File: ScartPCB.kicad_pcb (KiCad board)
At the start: 4 copper layers, 39.5 x 21 mm, 55 parts, among them J1 Conn_02x10_Odd_Even, Q1 BC847W, Q2 BC857W, U1 TPS61040DBVR

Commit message: Change it to work more like I want it to
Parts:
- removed C1: 4.7uF, Capacitor_SMD:C_0402_1005Metric
- removed C2: 10pF, Capacitor_SMD:C_0402_1005Metric
- removed C3: 1uF, Capacitor_SMD:C_0402_1005Metric
- removed C4: 100nF, Capacitor_SMD:C_0402_1005Metric
- removed CB2, CC2, CG2, CR2: 100uF, Capacitor_SMD:C_1206_3216Metric
- removed CB3, CC3, CG3, CR3: 22uF, Capacitor_SMD:C_0603_1608Metric
- removed D1, D2: D_Schottky, Diode_SMD:D_0402_1005Metric
- removed L1: 10uH, Inductor_SMD:L_0603_1608Metric
- removed Q1: BC847W, Package_TO_SOT_SMD:SOT-323_SC-70
- removed Q2: BC857W, Package_TO_SOT_SMD:SOT-323_SC-70
- removed R1: 1.6M, Resistor_SMD:R_0402_1005Metric
- removed R2: 200K, Resistor_SMD:R_0402_1005Metric
- removed R3: 1K, Resistor_SMD:R_0402_1005Metric
- removed R5, R6: 1M, Resistor_SMD:R_0402_1005Metric
- C0: footprint Capacitor_SMD:C_0402_1005Metric -> Capacitor_SMD:C_0805_2012Metric_Pad1.18x1.45mm_HandSolder
- CB1, CG1, CR1: value 100uF -> C_Polarized; footprint Capacitor_SMD:C_1206_3216Metric -> Capacitor_Tantalum_SMD:CP_EIA-3528-21_Kemet-B_HandSolder
- CC1: value 100uF -> 220uF; footprint Capacitor_SMD:C_1206_3216Metric -> Capacitor_Tantalum_SMD:CP_EIA-3528-21_Kemet-B_HandSolder
- R7, R9, RB1, RB2, RC2, RG1, RG2, RR1, RR2: footprint Resistor_SMD:R_0402_1005Metric -> Resistor_SMD:R_0805_2012Metric_Pad1.20x1.40mm_HandSolder
- R8: footprint Resistor_SMD:R_0402_1005Metric -> Resistor_SMD:R_0805_2012Metric_Pad1.20x1.40mm_HandSolder; moved to F.Cu
- RC1: value 300 -> 470; footprint Resistor_SMD:R_0402_1005Metric -> Resistor_SMD:R_0805_2012Metric_Pad1.20x1.40mm_HandSolder
- U1: value TPS61040DBVR -> 74LVC1G17; footprint Footprints:TPS61040DBVR -> Package_TO_SOT_SMD:SC-74A-5_1.55x2.9mm_P0.95mm
- moved U1 14.7 mm to (140.3, 115.0), turned to 180 degrees
- moved R9 12.1 mm to (148.5, 117.5)
- moved RR1 9.16 mm to (146.5, 114.0), turned to 180 degrees
- moved RG1 6.19 mm to (151.0, 114.0), turned to 180 degrees
- moved RC1 6.01 mm to (132.5, 116.5)
- moved RR2 5.63 mm to (143.5, 113.5), turned to -90 degrees
- moved RB1 5.58 mm to (158.0, 114.0), turned to 180 degrees
- moved CB1 4.36 mm to (158.6, 117.0), turned to 0 degrees
- moved RB2 4.29 mm to (151.5, 109.5)
- moved CR1 3.94 mm to (145.5, 117.0), turned to 0 degrees
- moved RG2 2.97 mm to (147.5, 111.5), turned to 0 degrees
- moved CG1 2.96 mm to (152.0, 117.0), turned to 0 degrees
- moved R7 2.36 mm to (136.0, 115.5)
- moved C0 2.25 mm to (156.5, 111.5), turned to 0 degrees
- moved R8 1.55 mm to (138.5, 116.0)
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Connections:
- J1 pad 13: unconnected-(J1-Pad13) -> GND
- J1 pad 14: unconnected-(J1-Pad14) -> GND
- J1 pad 4: unconnected-(J1-Pad4) -> GND
- J1 pad 5: unconnected-(J1-Pad5) -> GND
- J1 pad 8: SWITCH -> unconnected-(J1-Pin_8-Pad8)
- J1 pad 9: unconnected-(J1-Pad9) -> GND
- R7 pad 1: Net-(CC1-Pad2) -> Net-(CC1-Pad1)
- R8 pad 1: Net-(CC1-Pad2) -> Net-(CC1-Pad1)
- RC1 pad 2: Net-(CC1-Pad1) -> Net-(CC1-Pad2)
- U1 pad 1: Net-(D2-Pad2) -> unconnected-(U1-NC-Pad1)
- U1 pad 2: GND -> C
- U1 pad 3: Net-(C2-Pad2) -> GND
- U1 pad 4: Net-(C1-Pad1) -> C_SYNC
- U1 pad 5: Net-(C1-Pad1) -> +5V
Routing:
- net RGB_BLANKING: track 3.41 -> 14.5 mm
- net Net-(CC1-Pad2): track 13.2 -> 3.41 mm
- net Net-(JP2-B): track 14.3 -> 5.61 mm
- net B: track 8.77 -> 16.8 mm
- net Net-(C4-Pad2): track 7.12 -> 0.00 mm
- net RED: track 6.86 -> 13.9 mm
- net Net-(C1-Pad1): track 6.54 -> 0.00 mm
- net GREEN: track 6.68 -> 12.7 mm
- net Net-(CC1-Pad1): track 12.1 -> 6.52 mm
- net BLUE: track 6.68 -> 11.7 mm
- net Net-(C2-Pad1): track 4.66 -> 0.00 mm
- net Net-(C2-Pad2): track 4.48 -> 0.00 mm
- net Net-(D2-Pad2): track 3.85 -> 0.00 mm
- net SWITCH: track 3.66 -> 0.00 mm
- net Net-(CB1-Pad1): track 5.79 -> 3.00 mm
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- removed copper zone on B.Cu, net +5V
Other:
- board text added: "V1.0"
- board text added: "github/ dottedquad"
- board text removed: "V2.0"
- board text removed: "github/ screwbreaker"

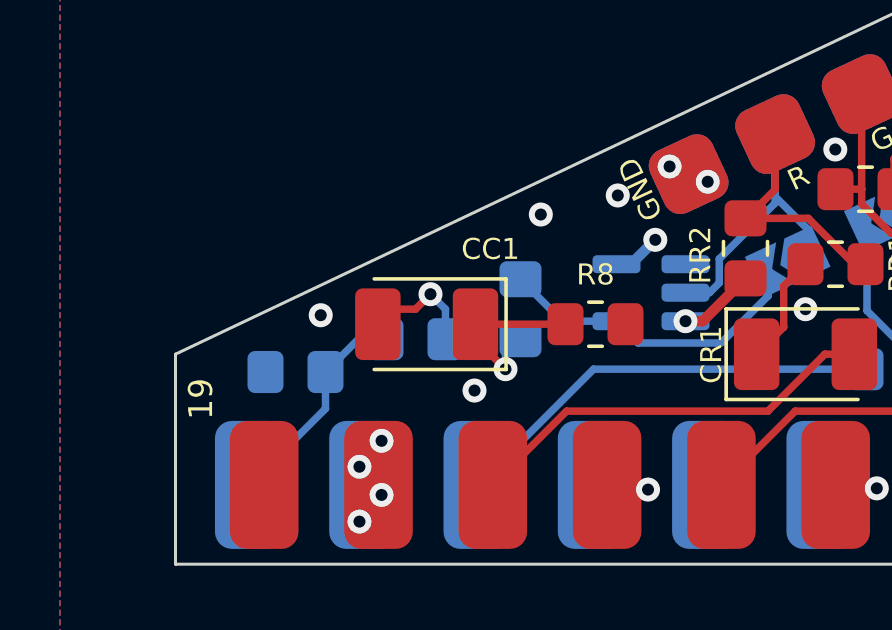
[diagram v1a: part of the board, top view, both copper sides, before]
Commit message: tweak position of csync cap
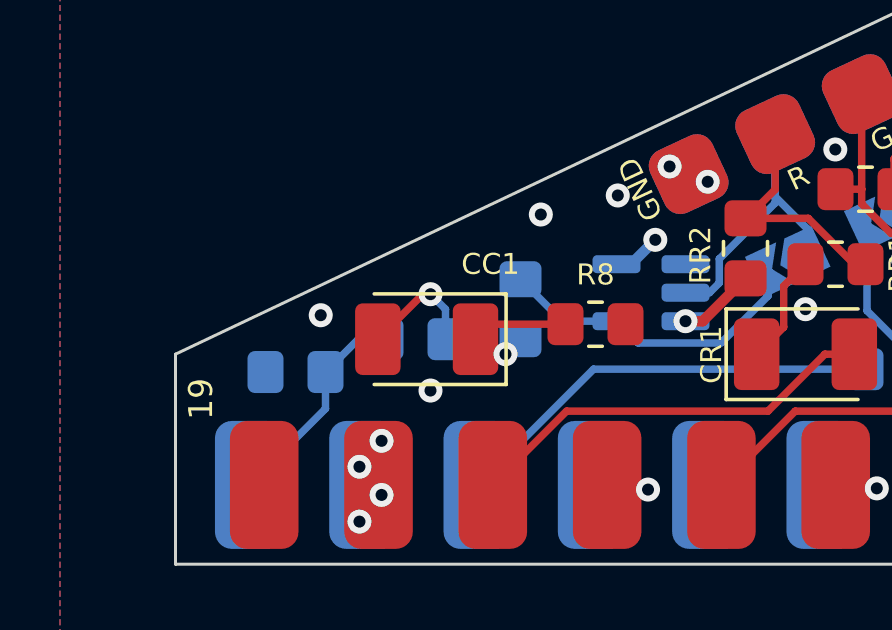
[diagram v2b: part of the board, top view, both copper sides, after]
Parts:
- moved CC1 0.50 mm to (132.9, 116.5)
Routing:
- net Net-(CC1-Pad1): track 6.52 -> 4.91 mm
- net Net-(CC1-Pad2): track 3.41 -> 4.08 mm

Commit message: Get ready for first run
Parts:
- added JI13: Conn_01x01, Footprints:PAD1.5x1.5, F.Cu at (128.0, 117.0)
- CB1, CG1, CR1: value C_Polarized -> 220uF
- moved C0 20.1 mm to (136.5, 113.5)
- moved R8 0.50 mm to (138.5, 116.5)
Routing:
- net +5V: track 6.10 -> 4.09 mm, vias 6 -> 7
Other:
- board text added: "Shld"
- board text added: "github/ dottedquad/ EasyScartPCB"
- board text removed: "github/ dottedquad"
